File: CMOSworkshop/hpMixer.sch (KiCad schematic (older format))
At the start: 23 parts, among them J1 JACK_STEREO, U4 TL082

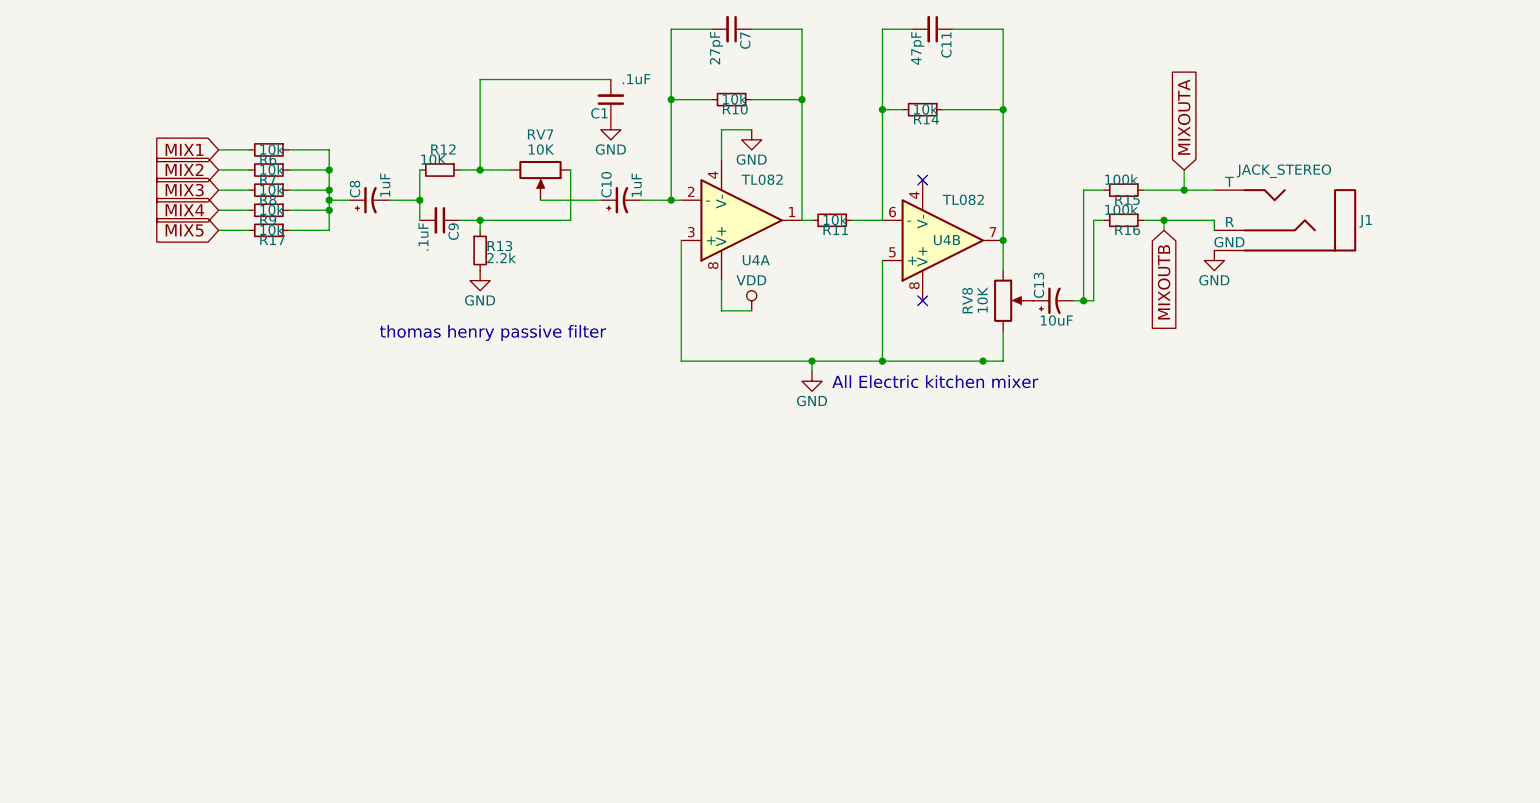
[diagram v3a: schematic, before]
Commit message: fixed mixer circuit.  separated passive filter for now.  may remove entirely..
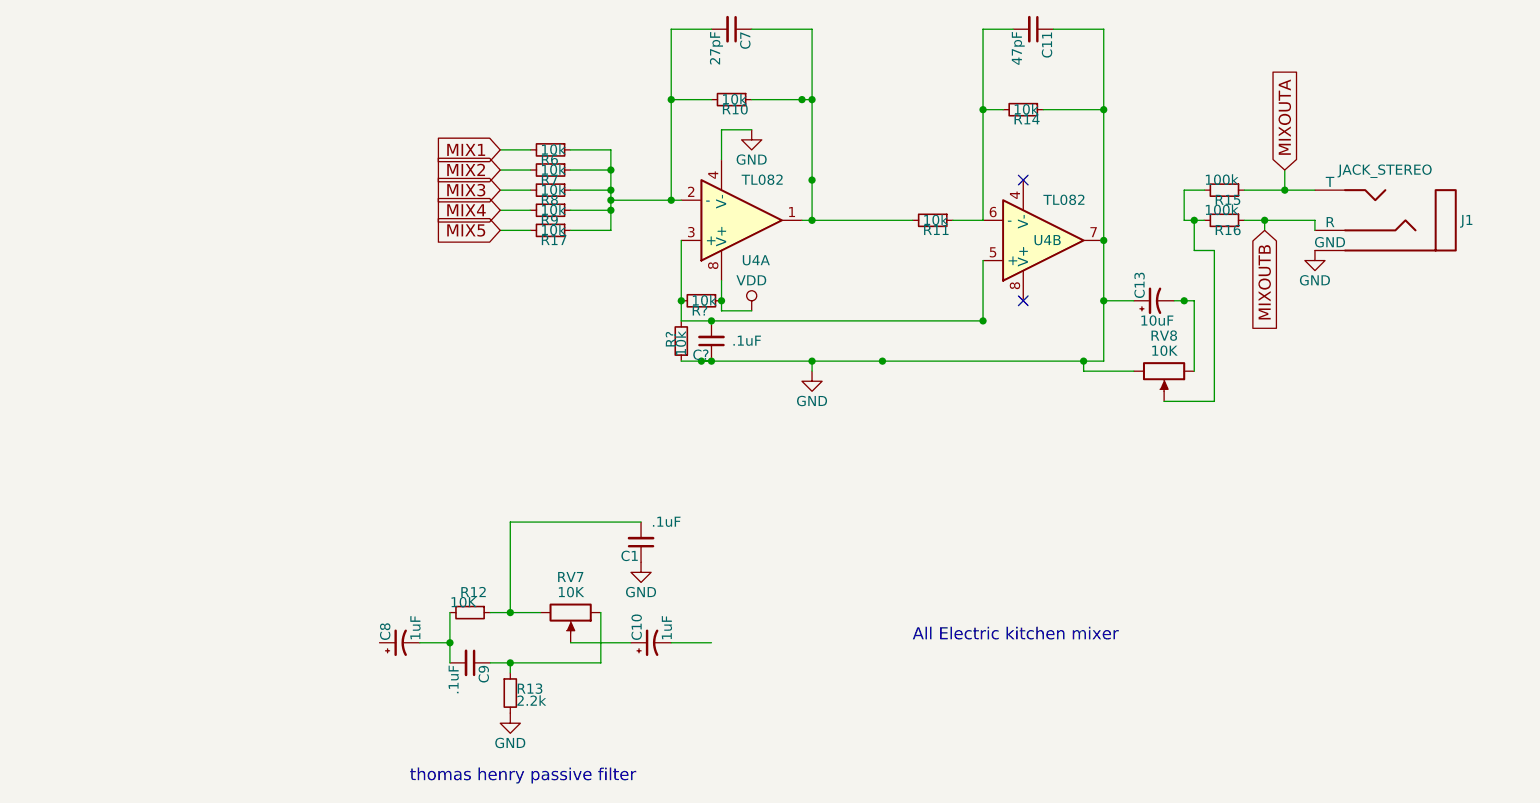
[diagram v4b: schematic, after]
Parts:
- added C?: .1uF, Capacitors_THT:CP_Radial_D5.0mm_P2.50mm, symbol C_Small
- added R? (x2): 10k, 4ms-footprints:R-TH, symbol R_Small-RESCUE-CMOSworkshop_ThinStrips
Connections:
- net GND: now also C11.1, C13.+, R14.1, U4.7, C?.1, R?.1; no longer U4.3 (+), U4.5 (+)
- net VDD: now also R?.1
- net at R17.1, R6.1, R7.1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: now also C7.2, R10.2, U4.2 (-); no longer C8.+
- net at RV8.2: now also R15.2, R16.2; no longer C13.+
- new net: C?.2, R?.2, R?.2, U4.3 (+), U4.5 (+)
- new net: C13.-, RV8.1
- now unconnected: C10.-
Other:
- moved on the sheet: C1, C10, C11, C13, C8, C9, J1, R11, R12, R13, R14, R15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

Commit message: changed touchpads to copper and adjusted for 2.54mm spacing
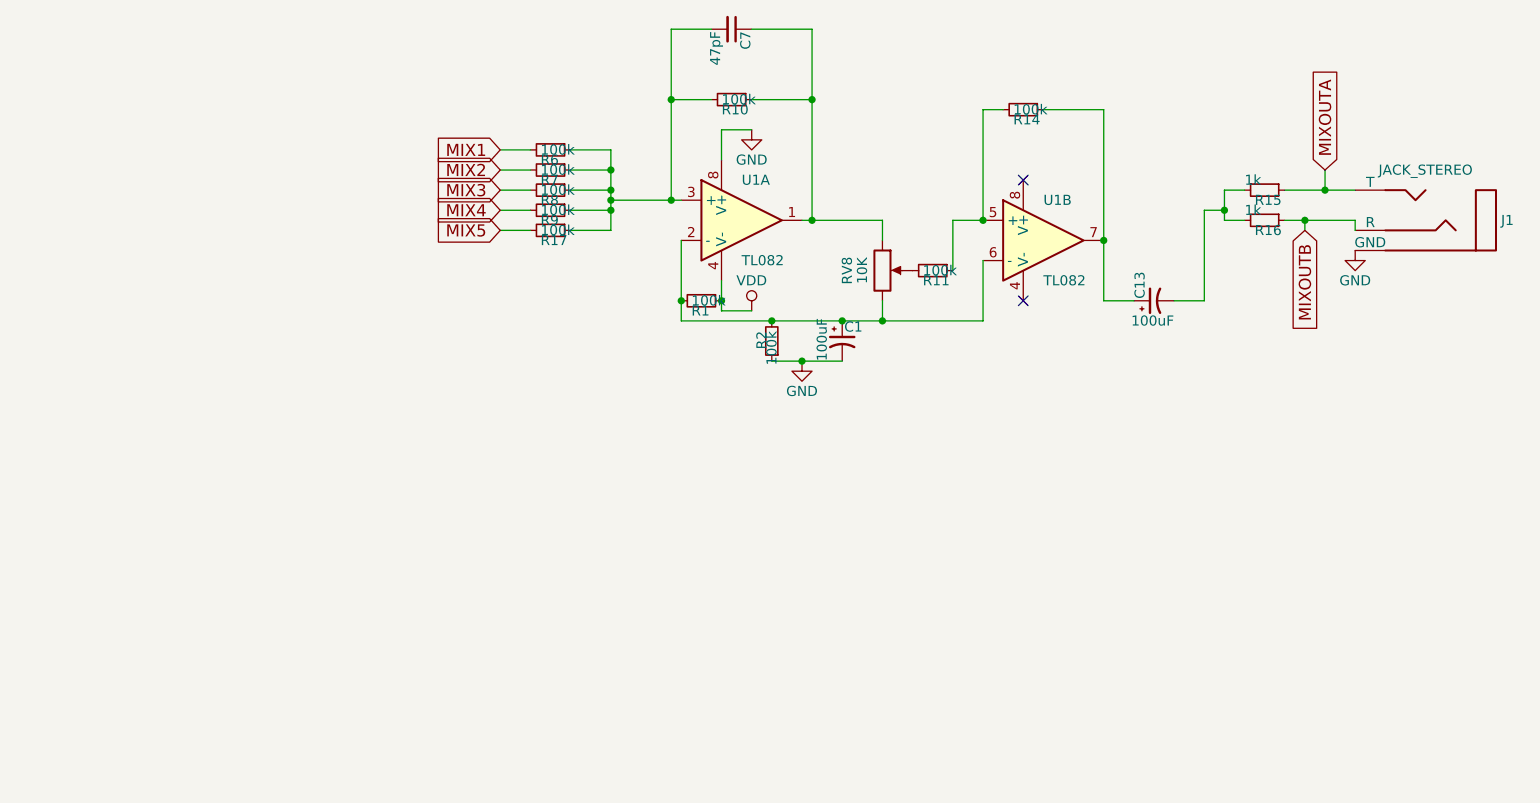
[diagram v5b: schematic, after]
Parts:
- removed C1, C9, C?: .1uF, Capacitors_THT:CP_Radial_D5.0mm_P2.50mm, symbol C_Small
- removed C10, C8: 1uF, Capacitors_THT:CP_Radial_D5.0mm_P2.50mm, symbol CP1_Small-RESCUE-CMOSworkshop_ThinStrips
- removed C11: 47pF, Capacitors_THT:C_Rect_L4.0mm_W2.5mm_P2.50mm, symbol C_Small
- removed R12: 10K, 4ms-footprints:R-TH, symbol R_Small-RESCUE-CMOSworkshop_ThinStrips
- removed R13: 2.2k, 4ms-footprints:R-TH, symbol R_Small-RESCUE-CMOSworkshop_ThinStrips
- removed RV7: 10K, 4ms-footprints:POT-9MM-ALPHA, symbol POT-RESCUE-CMOSworkshop_ThinStrips
- removed U4: TL082, Sockets_DIP:DIP-8__300, symbol TL082
- added C1: 100uF, Capacitors_ThroughHole:C_Radial_D5_L6_P2.5, symbol CP1_Small-RESCUE-CMOSworkshop_ThinStrips
- added U1: TL082, Sockets_DIP:DIP-8__300, symbol TL082
- C13: value 10uF -> 100uF; footprint Capacitors_THT:CP_Radial_D5.0mm_P2.50mm -> Capacitors_ThroughHole:C_Radial_D5_L6_P2.5
- C7: value 27pF -> 47pF
- R1, R2: renamed from R?; value 10k -> 100k
- R10, R11, R14, R17, R6, R7, R8, R9: value 10k -> 100k
- R15, R16: value 100k -> 1k
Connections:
- net GND: now also C1.-, U1.8 (V+); no longer C13.+, R14.1, RV8.3
- net VDD: now also U1.4 (V-)
- net at C7.2, R10.2, R17.1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: now also U1.3 (+)
- net at C7.1, R10.1: now also RV8.1, U1.1; no longer R11.2
- net at R1.2, R2.2: now also RV8.3, C1.+, U1.2 (-), U1.6 (-)
- net at R11.1, R14.2: now also U1.5 (+)
- net at C13.-: now also R15.2, R16.2; no longer RV8.1
- new net: R11.2, RV8.2
- new net: C13.+, R14.1, U1.7
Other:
- note removed: "All Electric kitchen mixer\n"
- note removed: "thomas henry passive filter\n"
- moved on the sheet: J1, R11, R15, R16, R2, RV8
